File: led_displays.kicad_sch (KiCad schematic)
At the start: 6 parts

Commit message: Mutimplex cat6 and cat7 conect decimal point on second diplay module
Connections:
- net 2_an15: now also DS4.7 (ANODE_DECIMAL_POINT)
- net 2_ca6: no longer DS4.9 (CATHODE_ROW_7)
- new net 2_ca7: DS4.9 (CATHODE_ROW_7)
- no-connect marks 1 -> 6
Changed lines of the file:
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@@
     (company "Andrew Tudoroi")
   )
+  (no_connect (at 57.15 40.64))
+  (no_connect (at 57.15 43.18))
+  (no_connect (at 59.69 146.05))
+  (no_connect (at 58.42 175.26))
+  (no_connect (at 58.42 172.72))
   (no_connect (at 58.42 120.65))
   (wire (pts (xy 123.19 95.25) (xy 128.27 95.25))
@@
     (stroke (width 0) (type default))
   )
-  (wire (pts (xy 123.19 172.72) (xy 128.27 172.72))
+  (wire (pts (xy 123.19 172.72) (xy 143.51 172.72))
     (stroke (width 0) (type default))
   )
@@
     (stroke (width 0) (type default))
   )
-  (wire (pts (xy 123.19 120.65) (xy 129.54 120.65))
-    (stroke (width 0) (type default))
-  )
   (wire (pts (xy 58.42 30.48) (xy 62.23 30.48))
     (stroke (width 0) (type default))
@@
     (stroke (width 0) (type default))
   )
+  (wire (pts (xy 123.19 120.65) (xy 143.51 120.65))
+    (stroke (width 0) (type default))
+  )
   (wire (pts (xy 123.19 38.1) (xy 130.81 38.1))
     (stroke (width 0) (type default))
@@
     (stroke (width 0) (type default))
   )
+  (wire (pts (xy 57.15 123.19) (xy 62.23 123.19))
+    (stroke (width 0) (type default))
+  )
   (wire (pts (xy 58.42 35.56) (xy 62.23 35.56))
     (stroke (width 0) (type default))
@@
     (stroke (width 0) (type default))
   )
-  (wire (pts (xy 123.19 146.05) (xy 127 146.05))
+  (wire (pts (xy 123.19 146.05) (xy 143.51 146.05))
     (stroke (width 0) (type default))
   )
@@
     )
   )
-  (global_label "2_ca6" (shape input) (at 128.27 172.72 0)
-    (effects (font (size 1.27 1.27)) (justify left))
-    (property "Intersheetrefs" "${INTERSHEET_REFS}" (at 128.27 172.72 0)
+  (global_label "2_ca6" (shape input) (at 143.51 172.72 0)
+    (effects (font (size 1.27 1.27)) (justify left))
+    (property "Intersheetrefs" "${INTERSHEET_REFS}" (at 143.51 172.72 0)
       (effects (font (size 1.27 1.27)) hide)
     )
@@
     )
   )
+  (global_label "2_ca7" (shape input) (at 143.51 120.65 0)
+    (effects (font (size 1.27 1.27)) (justify left))
+    (property "Intersheetrefs" "${INTERSHEET_REFS}" (at 143.51 120.65 0)
+      (effects (font (size 1.27 1.27)) hide)
+    )
+  )
   (global_label "ca1" (shape input) (at 129.54 60.96 0) (fields_autoplaced)
     (effects (font (size 1.27 1.27)) (justify left))
@@
     )
   )
+  (global_label "2_an15" (shape input) (at 57.15 123.19 180) (fields_autoplaced)
+    (effects (font (size 1.27 1.27)) (justify right))
+    (property "Intersheetrefs" "${INTERSHEET_REFS}" (at 47.2707 123.19 0)
+      (effects (font (size 1.27 1.27)) (justify right) hide)
+    )
+  )
   (global_label "2_an0" (shape input) (at 128.27 162.56 0)
     (effects (font (size 1.27 1.27)) (justify left))
@@
     )
   )
-  (global_label "2_ca6" (shape input) (at 127 146.05 0)
-    (effects (font (size 1.27 1.27)) (justify left))
-    (property "Intersheetrefs" "${INTERSHEET_REFS}" (at 127 146.05 0)
+  (global_label "2_ca6" (shape input) (at 143.51 146.05 0)
+    (effects (font (size 1.27 1.27)) (justify left))
+    (property "Intersheetrefs" "${INTERSHEET_REFS}" (at 143.51 146.05 0)
       (effects (font (size 1.27 1.27)) hide)
     )
@@
     )
   )
-  (global_label "2_ca6" (shape input) (at 129.54 120.65 0)
-    (effects (font (size 1.27 1.27)) (justify left))
-    (property "Intersheetrefs" "${INTERSHEET_REFS}" (at 129.54 120.65 0)
-      (effects (font (size 1.27 1.27)) hide)
-    )
-  )

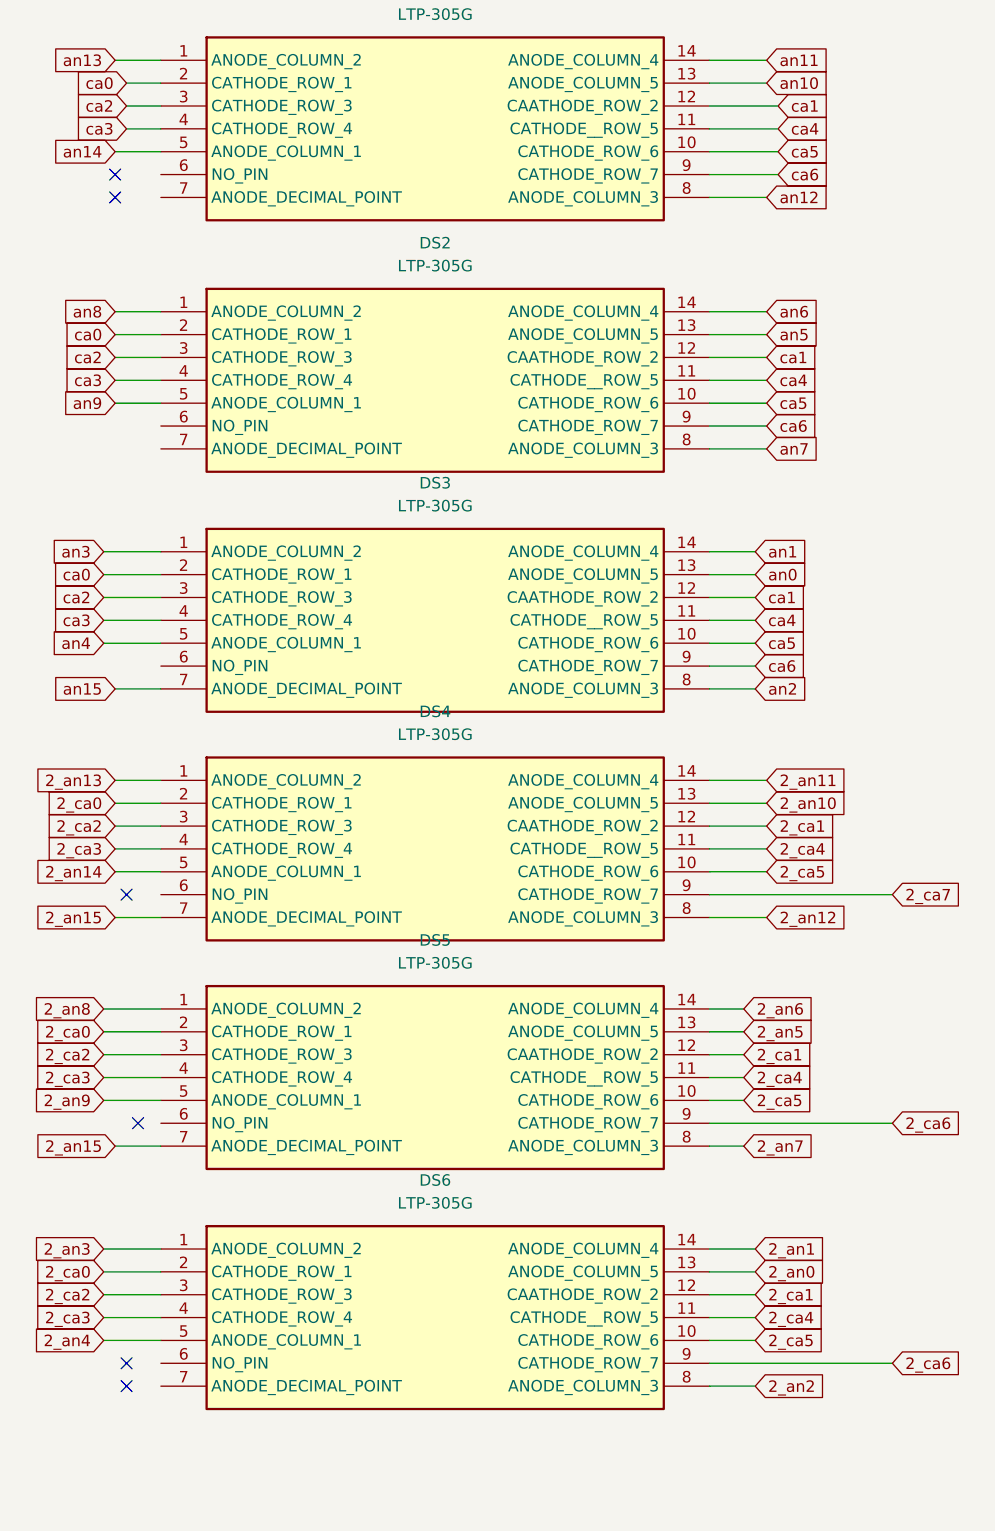
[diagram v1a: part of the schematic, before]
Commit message: Add second decimal connection to first led driver
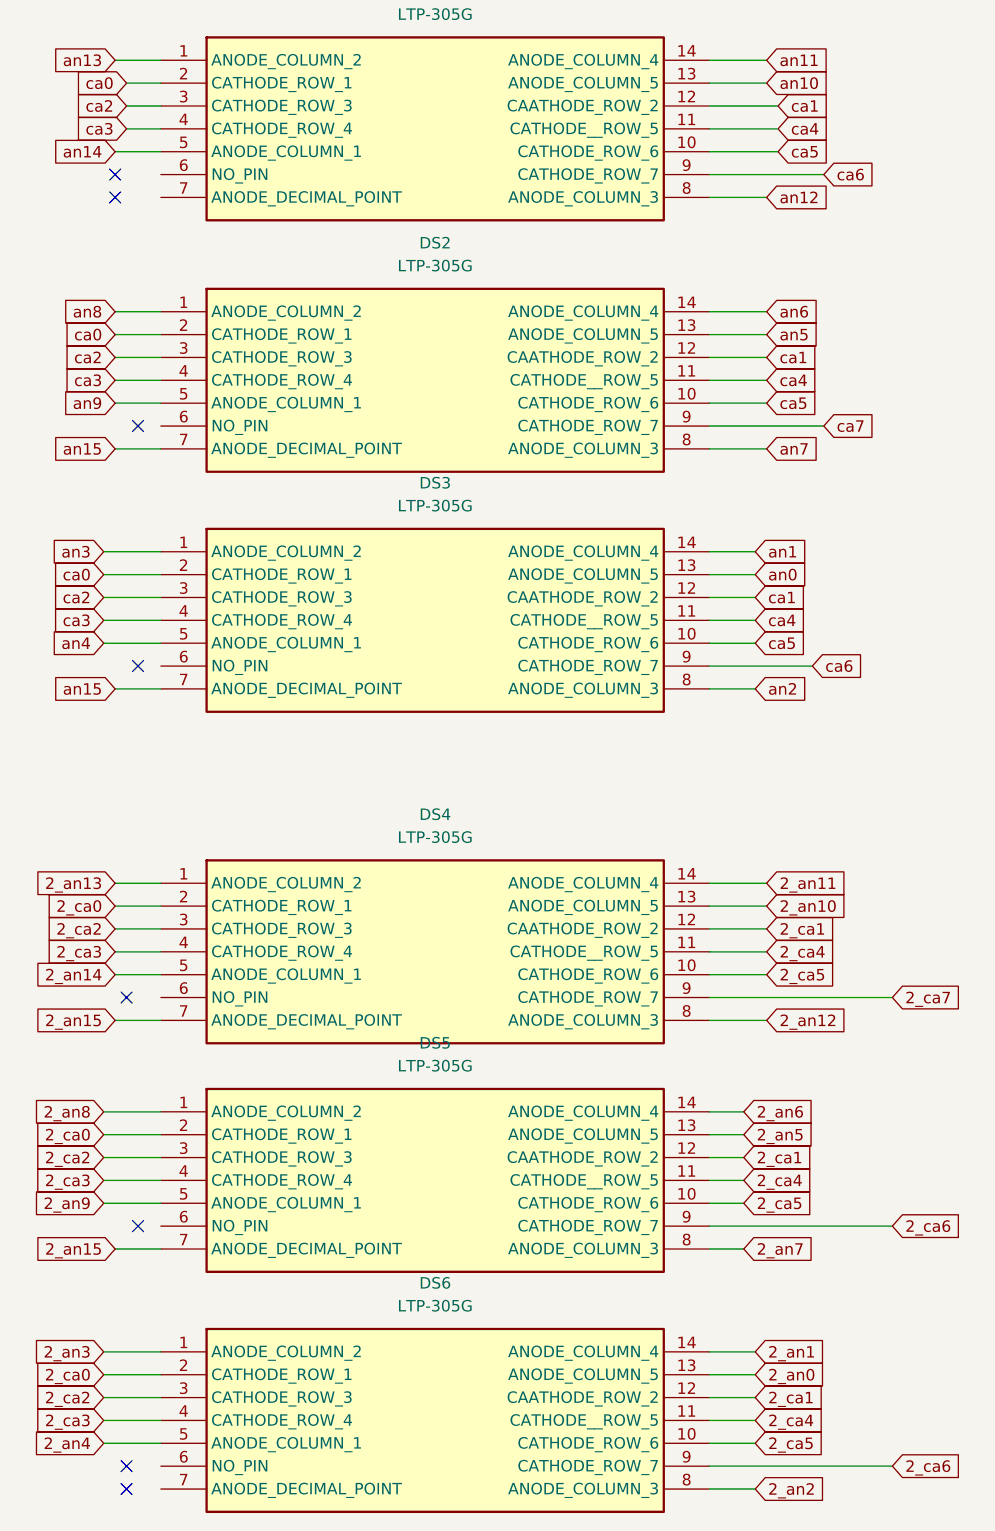
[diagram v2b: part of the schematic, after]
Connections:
- net an15: now also DS2.7 (ANODE_DECIMAL_POINT)
- net ca6: no longer DS2.9 (CATHODE_ROW_7)
- new net ca7: DS2.9 (CATHODE_ROW_7)
- no-connect marks 6 -> 8
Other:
- moved on the sheet: DS4, DS5, DS6

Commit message: Update library
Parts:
- DS1: footprint LTP-305G:DIPS762W50P254L1850H400Q14N -> Library:DIPS762W50P254L1850H400Q14N
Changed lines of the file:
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@@
       (effects (font (size 1.27 1.27)))
     )
-    (property "Footprint" "LTP-305G:DIPS762W50P254L1850H400Q14N" (at 119.38 122.86 0)
+    (property "Footprint" "Library:DIPS762W50P254L1850H400Q14N" (at 119.38 122.86 0)
       (effects (font (size 1.27 1.27)) (justify left top) hide)
     )

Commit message: Update ltp305 footprint
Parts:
- DS2, DS3, DS4, DS5, DS6: footprint LTP-305G:DIPS762W50P254L1850H400Q14N -> Library:DIPS762W50P254L1850H400Q14N
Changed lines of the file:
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@@
       (effects (font (size 1.27 1.27)))
     )
-    (property "Footprint" "LTP-305G:DIPS762W50P254L1850H400Q14N" (at 119.38 177.47 0)
+    (property "Footprint" "Library:DIPS762W50P254L1850H400Q14N" (at 119.38 177.47 0)
       (effects (font (size 1.27 1.27)) (justify left top) hide)
     )
@@
       (effects (font (size 1.27 1.27)))
     )
-    (property "Footprint" "LTP-305G:DIPS762W50P254L1850H400Q14N" (at 119.38 266.37 0)
+    (property "Footprint" "Library:DIPS762W50P254L1850H400Q14N" (at 119.38 266.37 0)
       (effects (font (size 1.27 1.27)) (justify left top) hide)
     )
@@
       (effects (font (size 1.27 1.27)))
     )
-    (property "Footprint" "LTP-305G:DIPS762W50P254L1850H400Q14N" (at 119.38 214.3 0)
+    (property "Footprint" "Library:DIPS762W50P254L1850H400Q14N" (at 119.38 214.3 0)
       (effects (font (size 1.27 1.27)) (justify left top) hide)
     )
@@
       (effects (font (size 1.27 1.27)))
     )
-    (property "Footprint" "LTP-305G:DIPS762W50P254L1850H400Q14N" (at 119.38 239.7 0)
+    (property "Footprint" "Library:DIPS762W50P254L1850H400Q14N" (at 119.38 239.7 0)
       (effects (font (size 1.27 1.27)) (justify left top) hide)
     )
@@
       (effects (font (size 1.27 1.27)))
     )
-    (property "Footprint" "LTP-305G:DIPS762W50P254L1850H400Q14N" (at 119.38 150.8 0)
-      (effects (font (size 1.27 1.27)) (justify left top) hide)
-    )
+    (property "Footprint" "Library:DIPS762W50P254L1850H400Q14N" (at 119.38 150.8 0)
+      (effects (font (size 1.27 1.27)) (justify left top) hide)
+    )

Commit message: Piatnag_5_bt
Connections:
- net 2_an14: now also DS6.7 (ANODE_DECIMAL_POINT)
- net 2_ca6: now also DS4.9 (CATHODE_ROW_7); no longer DS5.9 (CATHODE_ROW_7), DS6.9 (CATHODE_ROW_7)
- net 2_ca7: now also DS5.9 (CATHODE_ROW_7), DS6.9 (CATHODE_ROW_7); no longer DS4.9 (CATHODE_ROW_7)
- net an14: now also DS3.7 (ANODE_DECIMAL_POINT)
- net an15: now also DS1.7 (ANODE_DECIMAL_POINT); no longer DS3.7 (ANODE_DECIMAL_POINT)
- net ca6: no longer DS3.9 (CATHODE_ROW_7)
- net ca7: now also DS3.9 (CATHODE_ROW_7)
- no-connect marks 8 -> 6
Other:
- moved on the sheet: DS4, DS5, DS6
